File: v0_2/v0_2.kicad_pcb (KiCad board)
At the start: 2 copper layers, 9 parts, among them IC1 RASPBERRY_PI_PICO_W, IC2 PCF85063AT_AAZ, IC3 AP2138N-3.3TRG1, IC4 BH1745NUC-E2, Q1 DMG2301L-7, Q2 DMG2301L-7, Q3 DMG2301L-7, Q4 DMN3731U-7, U1 AHT20

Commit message: add sensor schematic
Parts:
- removed IC2: PCF85063AT_AAZ, LIB_PCF85063AT_AAZ:SOIC127P600X175-8N
- added J1: S2B-PH-SM4-TB_LF__SN_, S2B-PH-SM4-TB(LF)(SN):S2BPHSM4TBLFSN, F.Cu at (164.1, 100.9)
- added U2: PCF85063ATL, Package_DFN_QFN:DFN-10-1EP_2.6x2.6mm_P0.5mm_EP1.3x2.2mm, F.Cu at (148.6, 60.0)
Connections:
- IC1 pad 10: unconnected-(IC1-I2C1_SCL_/SPI0_TX/GP7-Pad10) -> /SWITCH_STATUS
- IC1 pad 11: unconnected-(IC1-UART1_TX/I2C0_SDA_/SPI1_RX/GP8-Pad11) -> /RTC_ALARM
- IC1 pad 30: unconnected-(IC1-RUN-Pad30) -> /RUN
- IC1 pad 36: unconnected-(IC1-3V3(OUT)-Pad36) -> +3.3V
- IC1 pad 39: unconnected-(IC1-VSYS-Pad39) -> VSYS
- IC1 pad 4: unconnected-(IC1-I2C1_SDA_/SPI0_SCK/GP2-Pad4) -> /HOLD_VSYS_EN
- IC1 pad 40: unconnected-(IC1-VBUS-Pad40) -> VBUS
- IC1 pad 5: unconnected-(IC1-I2C0_SCL_/SPI0_TX/GP3-Pad5) -> /I2C_INT/2.3B
- IC1 pad 6: unconnected-(IC1-UART1_TX/I2C0_SDA_/SPI0_RX/GP4-Pad6) -> /I2C_SDA/2.1B
- IC1 pad 7: unconnected-(IC1-UART1_RX/I2C0_SCL_/SPI0_CSN/GP5-Pad7) -> /I2C_SCL/2.1B
- IC1 pad 9: unconnected-(IC1-I2C1_SDA_/SPI0_SCK/GP6-Pad9) -> /ACT_LED
- IC3 pad 1: unconnected-(IC3-GND-Pad1) -> GND
- IC3 pad 2: unconnected-(IC3-VOUT-Pad2) -> +3.3V
- IC3 pad 3: unconnected-(IC3-VIN-Pad3) -> Net-(IC3-VIN)
- Q1 pad 1: unconnected-(Q1-Pad1) -> VBUS
- Q1 pad 2: unconnected-(Q1-Pad2) -> Net-(IC3-VIN)
- Q1 pad 3: unconnected-(Q1-Pad3) -> +BATT
- Q2 pad 1: unconnected-(Q2-Pad1) -> Net-(Q2-Pad1)
- Q2 pad 2: unconnected-(Q2-Pad2) -> Net-(IC3-VIN)
- Q2 pad 3: unconnected-(Q2-Pad3) -> VSYS
- Q3 pad 1: unconnected-(Q3-Pad1) -> Net-(U2-~{INT})
- Q3 pad 2: unconnected-(Q3-Pad2) -> V+_A0
- Q3 pad 3: unconnected-(Q3-Pad3) -> /RTC_ALARM
- Q4 pad 1: unconnected-(Q4-Pad1) -> /VSYS_EN
- Q4 pad 2: unconnected-(Q4-Pad2) -> GND
- Q4 pad 3: unconnected-(Q4-Pad3) -> Net-(Q2-Pad1)

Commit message: add color sensor
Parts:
- added IC2: BH1750FVI-TR, BH1750:WSOF6, F.Cu at (146.6, 93.5)
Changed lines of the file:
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@@
   (net 68 "/VSYS_EN")
   (net 69 "/ALARM_LED")
+  (net 70 "Net-(IC2-ADDR)")
+  (net 71 "/Color/I2C_SDA{slash}1.4C")
+  (net 72 "/Color/RESET")
+  (net 73 "/Color/I2C_SCL{slash}1.4C")
   (footprint "DMG2301L-7:SOT96P240X110-3N" (layer "F.Cu")
     (at 164.05 68.58)
@@
     )
   )
+  (footprint "BH1750:WSOF6" (layer "F.Cu")
+    (at 146.625 93.5)
+    (descr "WSOF6")
+    (tags "Integrated Circuit")
+    (property "Arrow Part Number" "BH1750FVI-TR")
+    (property "Arrow Price/Stock" "https://www.arrow.com/en/products/bh1750fvi-tr/rohm-semiconductor")
+    (property "Description" "Ambient Light Sensor,16bit,I2C,WSOF6I ROHM BH1750FVI-TR Ambient Light Sensor Unit Surface Mount")
+    (property "Height" "")
+    (property "Manufacturer_Name" "ROHM Semiconductor")
+    (property "Manufacturer_Part_Number" "BH1750FVI-TR")
+    (property "Mouser Part Number" "755-BH1750FVI-TR")
+    (property "Mouser Price/Stock" "https://www.mouser.co.uk/ProductDetail/ROHM-Semiconductor/BH1750FVI-TR?qs=phc6PQ%252BTPUNy88lRCs6mVA%3D%3D")
+    (property "Sheetfile" "BH1745NUC.kicad_sch")
+    (property "Sheetname" "Color")
+    (property "ki_description" "Ambient Light Sensor,16bit,I2C,WSOF6I ROHM BH1750FVI-TR Ambient Light Sensor Unit Surface Mount")
+    (attr smd)
+    (fp_text reference "IC2" (at -0.357 -0.055) (layer "F.SilkS")
+        (effects (font (size 1.27 1.27) (thickness 0.254)))
+    )
+    (fp_text value "BH1750FVI-TR" (at -0.357 -0.055) (layer "F.SilkS") hide
+        (effects (font (size 1.27 1.27) (thickness 0.254)))
+    )
+    (fp_text user "${REFERENCE}" (at -0.357 -0.055) (layer "F.Fab")
+        (effects (font (size 1.27 1.27) (thickness 0.254)))
+    )
+    (fp_line (start -1.3 -0.8) (end 1.3 -0.8)
+      (stroke (width 0.2) (type solid)) (layer "F.SilkS"))
+    (fp_line (start 1.3 0.8) (end -1.3 0.8)
+      (stroke (width 0.2) (type solid)) (layer "F.SilkS"))
+    (fp_circle (center -1.811 -0.516) (end -1.811 -0.49703)
+      (stroke (width 0.2) (type solid)) (fill none) (layer "F.SilkS"))
+    (fp_line (start -1.3 -0.8) (end 1.3 -0.8)
+      (stroke (width 0.2) (type solid)) (layer "F.Fab"))
+    (fp_line (start -1.3 0.8) (end -1.3 -0.8)
+      (stroke (width 0.2) (type solid)) (layer "F.Fab"))
+    (fp_line (start 1.3 -0.8) (end 1.3 0.8)
+      (stroke (width 0.2) (type solid)) (layer "F.Fab"))
+    (fp_line (start 1.3 0.8) (end -1.3 0.8)
+      (stroke (width 0.2) (type solid)) (layer "F.Fab"))
+    (pad "1" smd rect (at -1.375 -0.5 90) (size 0.25 0.55) (layers "F.Cu" "F.Paste" "F.Mask")
+      (net 36 "+3.3V") (pinfunction "VCC") (pintype "passive"))
+    (pad "2" smd rect (at -1.375 0 90) (size 0.25 0.55) (layers "F.Cu" "F.Paste" "F.Mask")
+      (net 70 "Net-(IC2-ADDR)") (pinfunction "ADDR") (pintype "passive"))
+    (pad "3" smd rect (at -1.375 0.5 90) (size 0.25 0.55) (layers "F.Cu" "F.Paste" "F.Mask")
+      (net 41 "GND") (pinfunction "GND") (pintype "passive"))
+    (pad "4" smd rect (at 1.375 0.5 90) (size 0.25 0.55) (layers "F.Cu" "F.Paste" "F.Mask")
+      (net 71 "/Color/I2C_SDA{slash}1.4C") (pinfunction "SDA") (pintype "passive"))
+    (pad "5" smd rect (at 1.375 0 90) (size 0.25 0.55) (layers "F.Cu" "F.Paste" "F.Mask")
+      (net 72 "/Color/RESET") (pinfunction "DVI") (pintype "passive"))
+    (pad "6" smd rect (at 1.375 -0.5 90) (size 0.25 0.55) (layers "F.Cu" "F.Paste" "F.Mask")
+      (net 73 "/Color/I2C_SCL{slash}1.4C") (pinfunction "SCL") (pintype "passive"))
+    (model "BH1750FVI-TR.stp"
+      (offset (xyz 0.009999999626 -0.02999999888 0.1500000037))
+      (scale (xyz 1 1 1))
+      (rotate (xyz 90 0 0))
+    )
+  )

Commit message: schematic for enviro done
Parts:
- removed IC4: BH1745NUC-E2, BH1745NUC:SON50P210X200X60-9N
- added D3: 1PS88SB48, Package_TO_SOT_SMD:SOT-363_SC-70-6, F.Cu at (177.5, 86.4)
- added S1: TS-1101-C-W, TS-1101-C-W:TS1101CW, F.Cu at (136.0, 58.4)
- added S2: TS-1101-C-W, TS-1101-C-W:TS1101CW, F.Cu at (181.7, 78.7)
- Q4: value DMN3731U-7 -> DMN3731U-13
- moved IC3 5.08 mm to (158.7, 92.4)
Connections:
- IC1 pad 12: unconnected-(IC1-UART1_RX/I2C0_SCL_/SPI1_CSN/GP9-Pad12) -> /RESET
- IC2 pad 4: /Color/I2C_SDA/1.4C -> /I2C_SDA/2.1B
- IC2 pad 5: /Color/RESET -> /RESET
- IC2 pad 6: /Color/I2C_SCL/1.4C -> /I2C_SCL/2.1B
- IC3 pad 2: +3.3V -> V+_A0
- U1 pad 2: unconnected-(U1-VDD-Pad2) -> Net-(U1-VDD)
- U1 pad 3: unconnected-(U1-SCL-Pad3) -> /I2C_SCL/2.1B
- U1 pad 4: unconnected-(U1-SDA-Pad4) -> /I2C_SDA/2.1B
- U1 pad 5: unconnected-(U1-GND-Pad5) -> GND

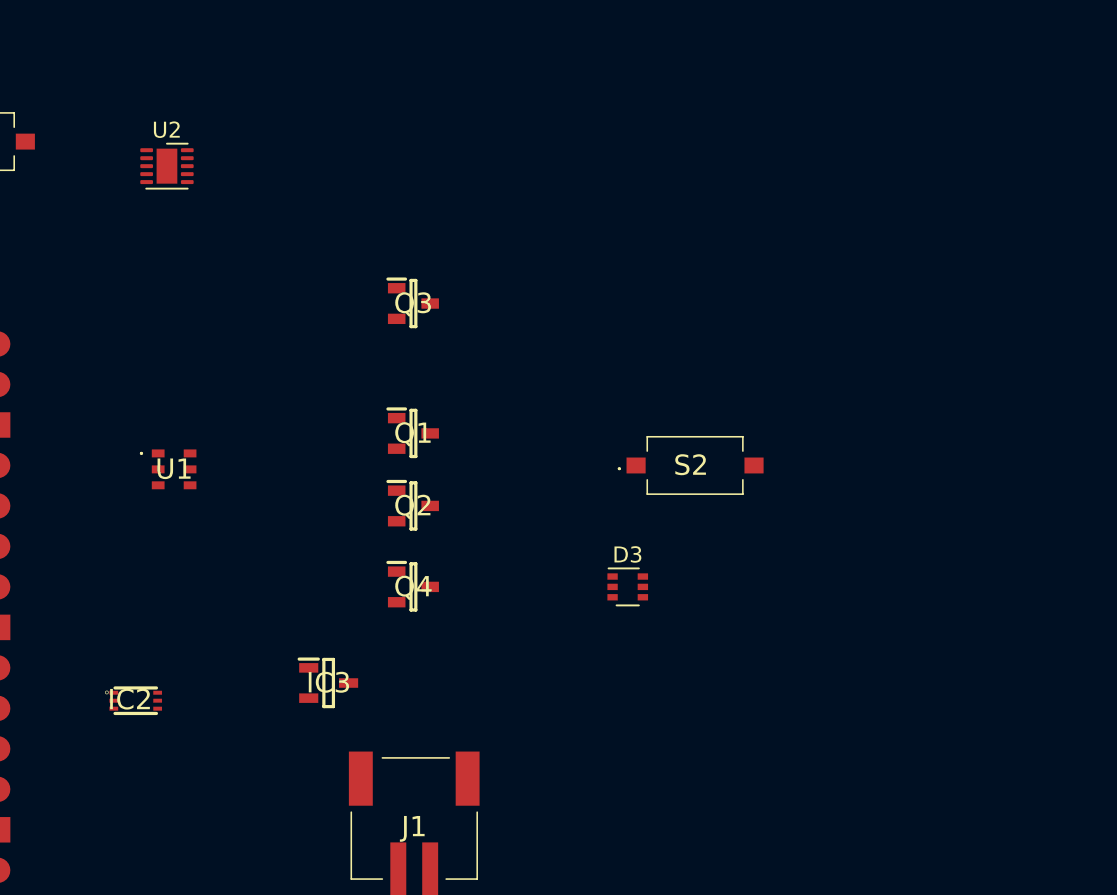
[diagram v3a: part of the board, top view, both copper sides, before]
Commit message: all part are added
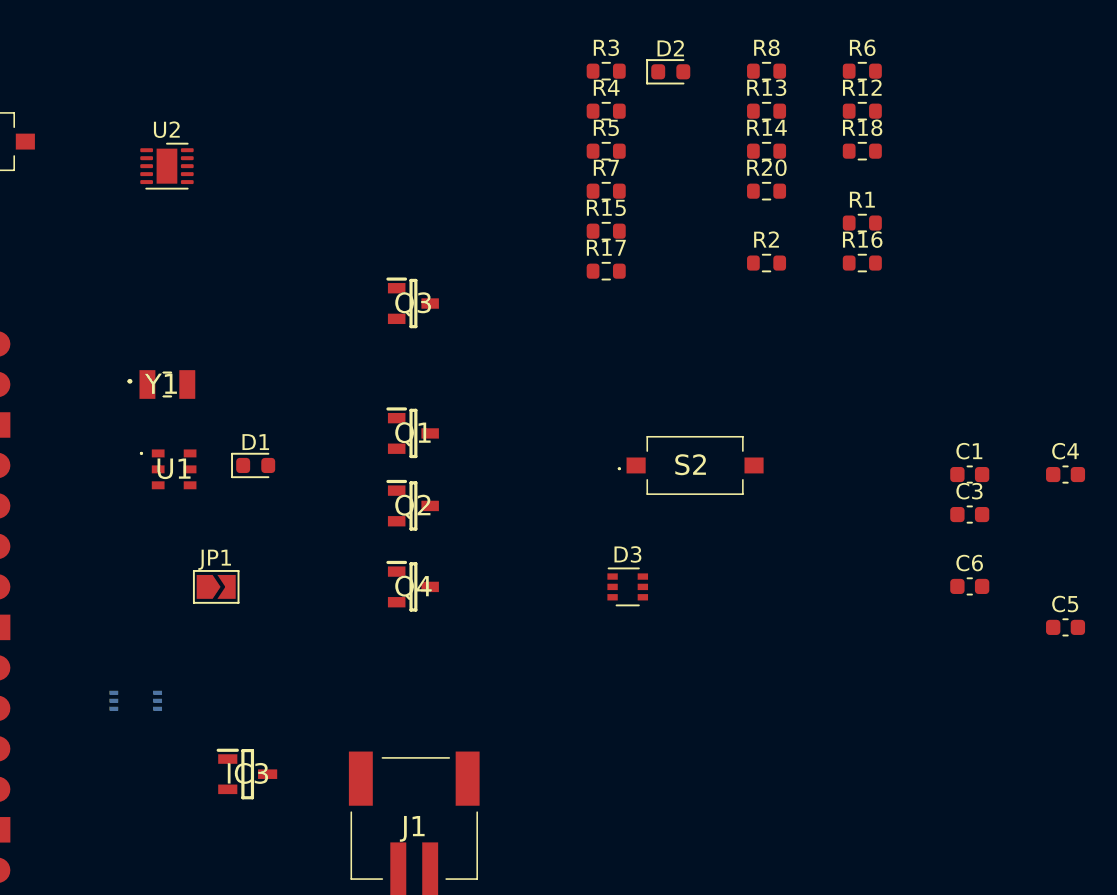
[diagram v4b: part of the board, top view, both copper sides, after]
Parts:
- added C1: 1uF, Capacitor_SMD:C_0603_1608Metric, F.Cu at (199.0, 79.3)
- added C3: 1uF, Capacitor_SMD:C_0603_1608Metric, F.Cu at (199.0, 81.8)
- added C4: 1uF, Capacitor_SMD:C_0603_1608Metric, F.Cu at (205.0, 79.3)
- added C5: 0.1uF, Capacitor_SMD:C_0603_1608Metric, F.Cu at (205.0, 88.9)
- added C6: 1uF, Capacitor_SMD:C_0603_1608Metric, F.Cu at (199.0, 86.3)
- added D1: WhiteLED, LED_SMD:LED_0603_1608Metric, F.Cu at (154.2, 78.7)
- added D2: RedLED, LED_SMD:LED_0603_1608Metric, F.Cu at (180.2, 54.0)
- added JP1: SolderJumper_2_Open, Jumper:SolderJumper-2_P1.3mm_Open_TrianglePad1.0x1.5mm, F.Cu at (151.7, 86.4)
- added R1: 120K, Resistor_SMD:R_0603_1608Metric, F.Cu at (192.2, 63.5)
- added R12: 220, Resistor_SMD:R_0603_1608Metric, F.Cu at (192.2, 56.5)
- added R13: 10K, Resistor_SMD:R_0603_1608Metric, F.Cu at (186.2, 56.5)
- added R14: 10K, Resistor_SMD:R_0603_1608Metric, F.Cu at (186.2, 59.0)
- added R15: 620K, Resistor_SMD:R_0603_1608Metric, F.Cu at (176.1, 64.0)
- added R16: 120K, Resistor_SMD:R_0603_1608Metric, F.Cu at (192.2, 66.0)
- added R17: 1K, Resistor_SMD:R_0603_1608Metric, F.Cu at (176.1, 66.5)
- added R18: 10K, Resistor_SMD:R_0603_1608Metric, F.Cu at (192.2, 59.0)
- added R2: 120K, Resistor_SMD:R_0603_1608Metric, F.Cu at (186.2, 66.0)
- added R20: 10K, Resistor_SMD:R_0603_1608Metric, F.Cu at (186.2, 61.5)
- added R3: 10K, Resistor_SMD:R_0603_1608Metric, F.Cu at (176.1, 54.0)
- added R4: 10K, Resistor_SMD:R_0603_1608Metric, F.Cu at (176.1, 56.5)
- added R5: 10K, Resistor_SMD:R_0603_1608Metric, F.Cu at (176.1, 59.0)
- added R6: 10K, Resistor_SMD:R_0603_1608Metric, F.Cu at (192.2, 54.0)
- added R7: 1K, Resistor_SMD:R_0603_1608Metric, F.Cu at (176.1, 61.5)
- added R8: 1K, Resistor_SMD:R_0603_1608Metric, F.Cu at (186.2, 54.0)
- added Y1: Q13FC1350000200, Q13FC1350000200:Q13FC1350000200, F.Cu at (148.6, 73.7)
- IC2: moved to B.Cu
- Q4: footprint DMG2301L-7:SOT96P240X110-3N -> DMN3731U-13:SOT96P240X110-3N
- moved IC3 7.65 mm to (153.7, 98.1)
- turned IC2 to 180 degrees
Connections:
- U2 pad 5: unconnected-(U2-VSS-Pad5) -> GND

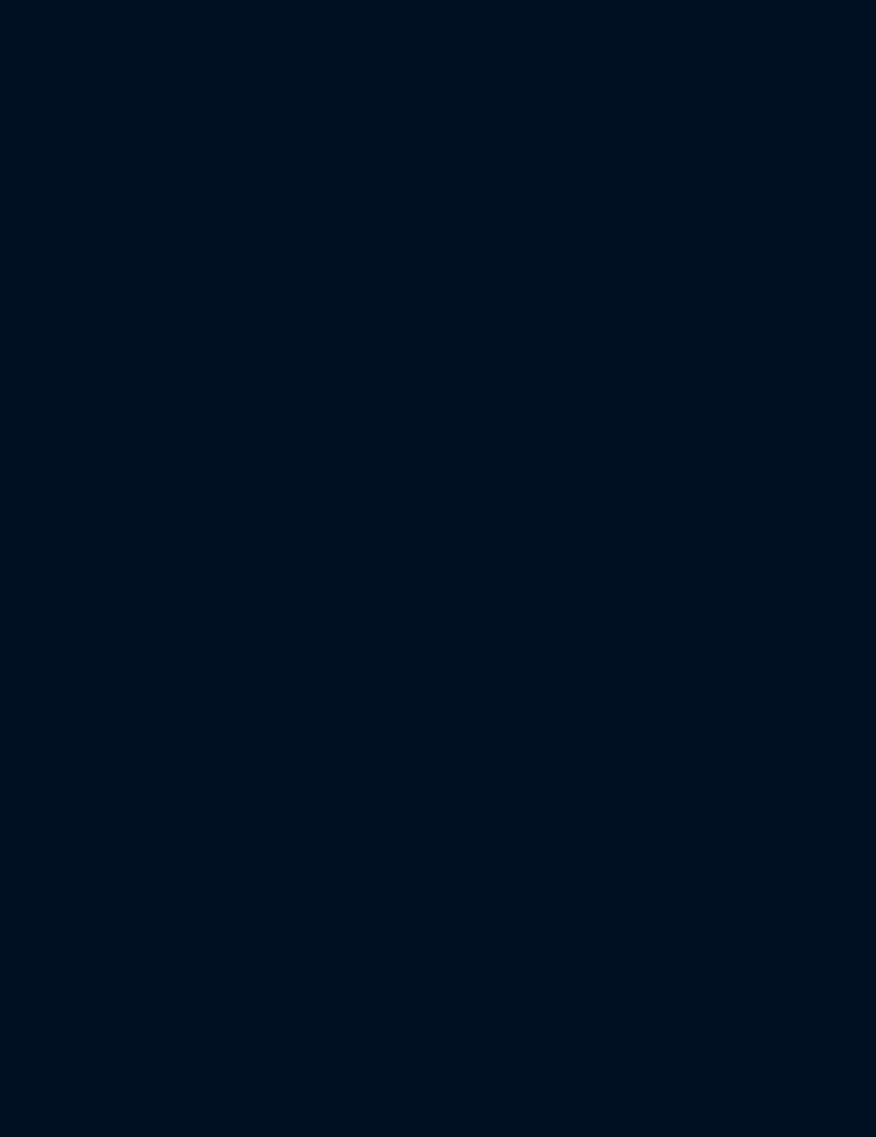
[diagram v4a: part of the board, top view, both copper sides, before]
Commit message: add sdcard socket
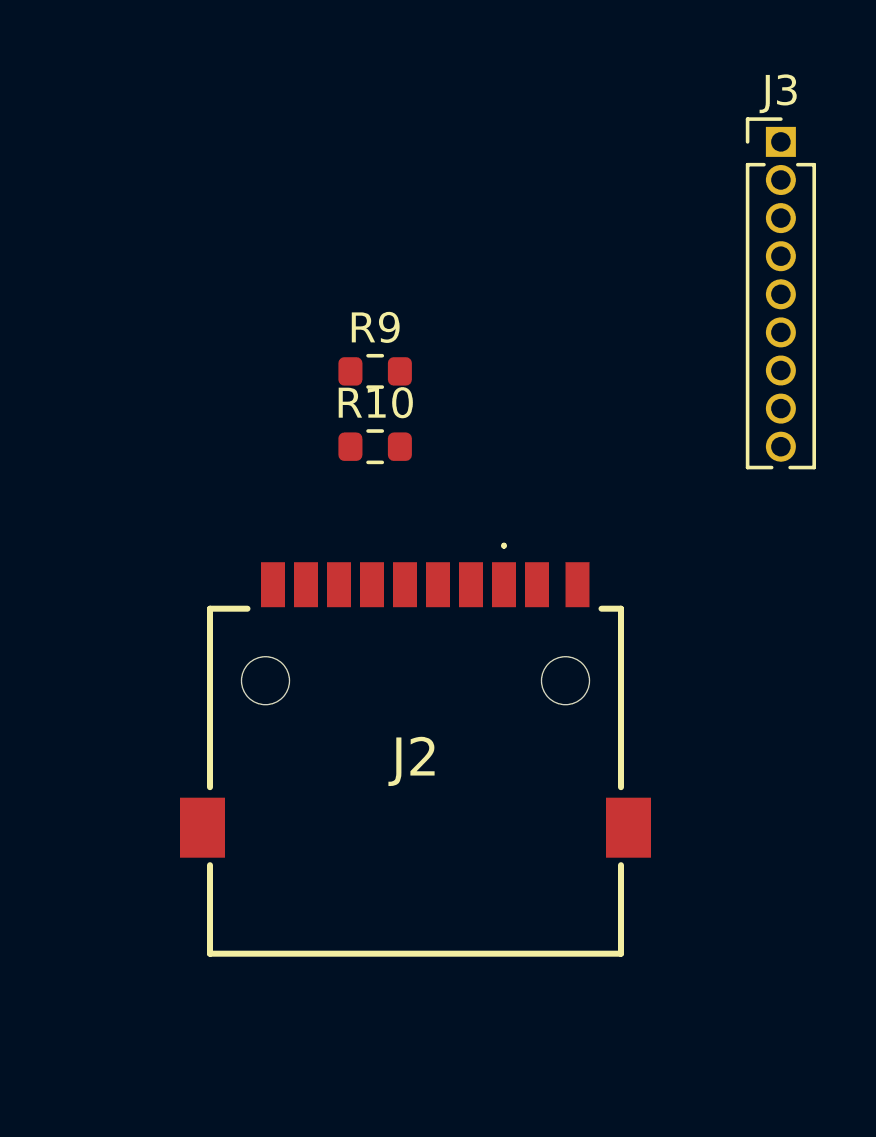
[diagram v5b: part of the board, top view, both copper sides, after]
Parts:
- added J2: HYCW110-TF10-180B, HYCW110-TF10-180B:HYCW110TF10180B, F.Cu at (208.8, 64.5)
- added J3: Conn_01x09_Pin, Connector_PinHeader_1.27mm:PinHeader_1x09_P1.27mm_Vertical, F.Cu at (221.0, 43.2)
- added R10: 47K, Resistor_SMD:R_0603_1608Metric, F.Cu at (207.5, 53.3)
- added R9: 47K, Resistor_SMD:R_0603_1608Metric, F.Cu at (207.5, 50.8)
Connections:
- IC1 pad 11: /RTC_ALARM -> /DO
- IC1 pad 12: /RESET -> /CS
- IC1 pad 14: unconnected-(IC1-I2C1_SDA_/SPI1__SCK/GP10-Pad14) -> /SCK
- IC1 pad 15: unconnected-(IC1-I2C1_SCL_/SPI1__TX/GP11-Pad15) -> /DIN
- IC1 pad 19: unconnected-(IC1-I2C1_SDA/SPI1_SCK/GP14-Pad19) -> /RTC_ALARM
- IC1 pad 20: unconnected-(IC1-I2C1_SCL/SPI1_TX/GP15-Pad20) -> /RESET

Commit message: for quoate
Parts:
- added H1: MountingHole_Pad, MountingHole:MountingHole_2.2mm_M2_Pad_TopBottom, F.Cu at (-14.9, -31.9)
- added H2: MountingHole_Pad, MountingHole:MountingHole_2.2mm_M2_Pad_TopBottom, F.Cu at (15.1, -32.1)
- added H3: MountingHole_Pad, MountingHole:MountingHole_2.2mm_M2_Pad_TopBottom, F.Cu at (-14.9, 31.9)
- added H4: MountingHole_Pad, MountingHole:MountingHole_2.2mm_M2_Pad_TopBottom, F.Cu at (15.0, 31.6)
- IC1, J1, S1: moved to B.Cu
- IC2: moved to F.Cu
- moved C1 224.9 mm to (-6.84, -11.4)
- moved C5 223.9 mm to (-7.62, 18.6), turned to -90 degrees
- moved C3 223.9 mm to (-6.84, -6.35)
- moved J2 222.1 mm to (6.35, -26.9), turned to 90 degrees
- moved C4 218.6 mm to (1.40, -0.30)
- moved S2 217.6 mm to (-14.0, -16.5), turned to 90 degrees
- moved R10 214.7 mm to (4.30, -16.0), turned to 90 degrees
- moved J3 213.9 mm to (15.2, -15.2)
- moved J1 212.9 mm to (-8.18, -24.1), turned to 90 degrees
- moved R9 211.0 mm to (7.30, -16.0), turned to 90 degrees
- moved R6 210.3 mm to (-14.9, 17.5), turned to -90 degrees
- moved R16 208.6 mm to (-2.98, -7.62)
- moved R17 204.8 mm to (-3.88, -31.1)
- moved R12 203.8 mm to (-7.20, 14.6), turned to 90 degrees
- moved C6 203.5 mm to (6.67, 19.6), turned to 180 degrees
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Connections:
- net /DIN renamed /MOSI
- net /DO renamed /MISO
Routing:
- net +3.3V: track 0.00 -> 135.3 mm, vias 0 -> 1
- net /MOSI: track 0.00 -> 68.0 mm
- net /CS: track 0.00 -> 67.8 mm
- net /RESET: track 0.00 -> 64.0 mm, vias 0 -> 1
- net /MISO: track 0.00 -> 62.6 mm, vias 0 -> 1
- net /ACT_LED: track 0.00 -> 55.2 mm, vias 0 -> 1
- net /I2C_SCL/2.1B: track 0.00 -> 52.4 mm, vias 0 -> 2
- net /SCK: track 0.00 -> 51.9 mm, vias 0 -> 1
- net V+_A0: track 0.00 -> 51.0 mm
- net /RTC_ALARM: track 0.00 -> 49.2 mm, vias 0 -> 2
- net /SWITCH_STATUS: track 0.00 -> 48.6 mm, vias 0 -> 2
- net /I2C_SDA/2.1B: track 0.00 -> 47.9 mm, vias 0 -> 1
- net VBUS: track 0.00 -> 47.2 mm, vias 0 -> 1
- net VSYS: track 0.00 -> 44.1 mm, vias 0 -> 1
- net /ALARM_LED: track 0.00 -> 40.0 mm, vias 0 -> 2
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- added copper zone on F.Cu, net GND
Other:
- board outline added: 36 x 70 mm
